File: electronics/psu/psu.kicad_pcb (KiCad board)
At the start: 2 copper layers, 100 x 100 mm, 65 parts, among them J1 Conn_01x03_Female, J2 control board, J3 processing, J4 processing, J5 pedals, J6 FAN, Q1 PHB21N06LT, U1 MC7815, U2 MC7915, U3 MIC4684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

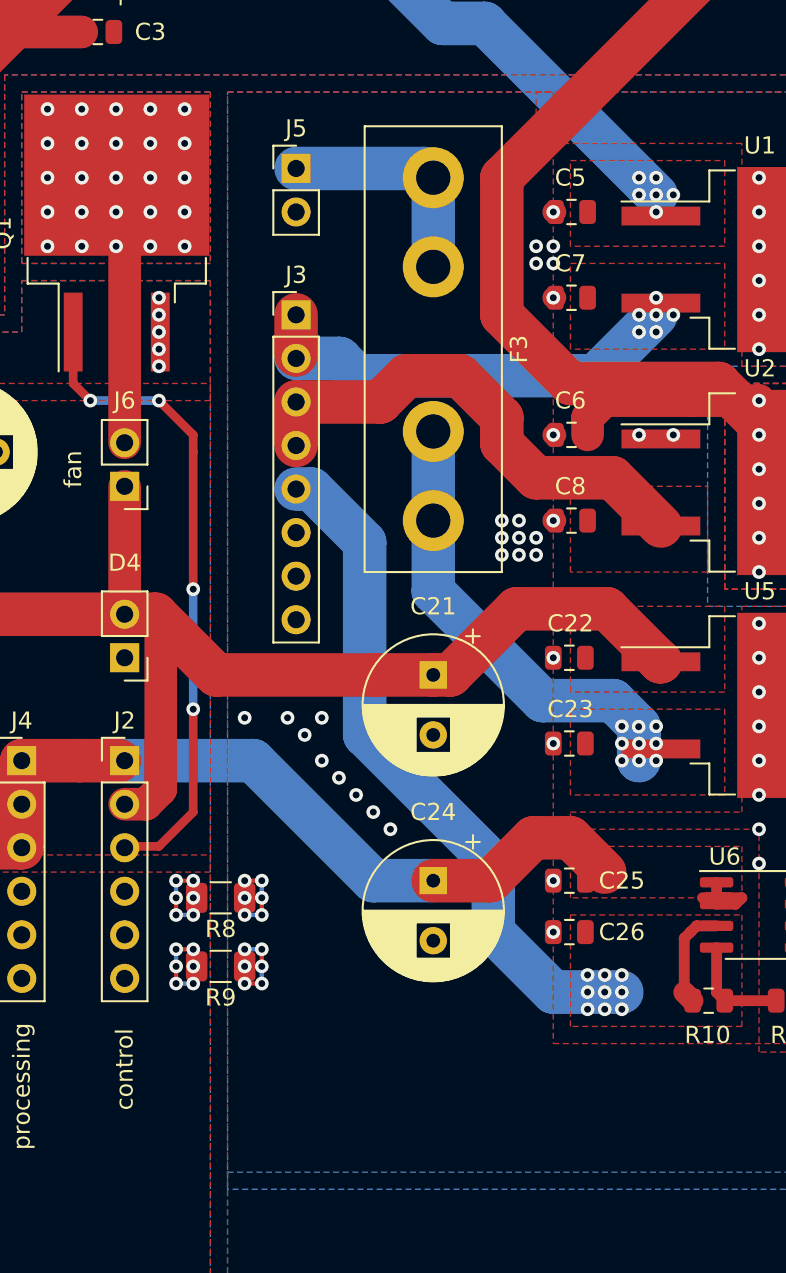
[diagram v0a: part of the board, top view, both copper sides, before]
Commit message: Changement de la fuse pour le 9v par une efuse
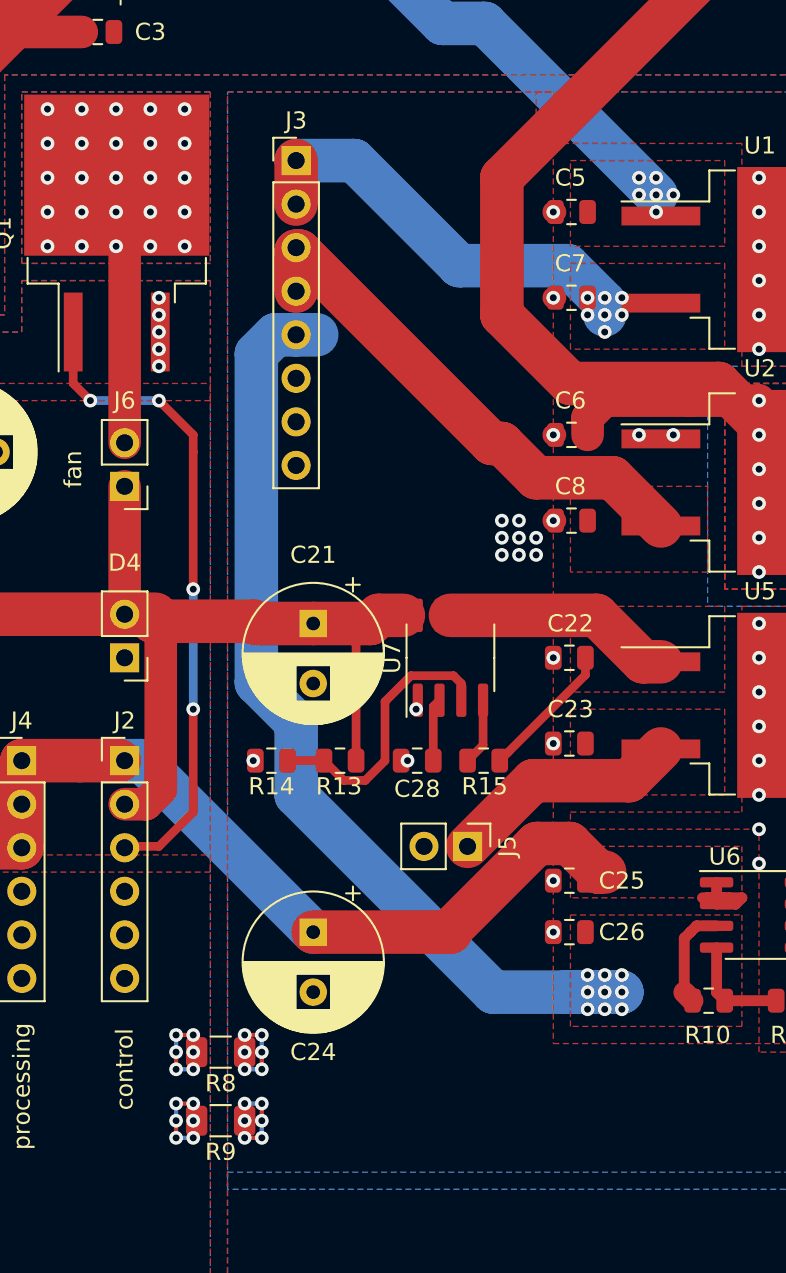
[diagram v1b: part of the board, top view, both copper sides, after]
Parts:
- removed F3: 0.5A, bass_amplifier:M205_FUSE
- added C28: C, Capacitor_SMD:C_0805_2012Metric, F.Cu at (90.1, 89.0)
- added R13: inf, Resistor_SMD:R_0805_2012Metric, F.Cu at (85.6, 89.0)
- added R14: inf, Resistor_SMD:R_0805_2012Metric, F.Cu at (81.6, 89.0)
- added R15: 309, Resistor_SMD:R_0805_2012Metric, F.Cu at (93.9, 89.0)
- added U7: NIS5112, Package_SO:SOIC-8_3.9x4.9mm_P1.27mm, F.Cu at (92.0, 83.0)
- moved J5 40.8 mm to (93.0, 94.0), turned to 270 degrees
- moved J3 9.00 mm to (83.0, 54.0)
- moved R8 9.00 mm to (78.6, 106.0)
- moved R9 9.00 mm to (78.6, 110.0)
- moved C21 7.62 mm to (84.0, 81.0)
- moved C24 7.62 mm to (84.0, 99.0)
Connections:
- C22 pad 1: /D+12V -> Net-(C22-Pad1)
- C23 pad 1: Net-(C23-Pad1) -> /A+9V
- U5 pad 1: /D+12V -> Net-(C22-Pad1)
- U5 pad 3: Net-(C23-Pad1) -> /A+9V
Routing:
- net Net-(C23-Pad1): track 27.6 -> 0.00 mm, vias 9 -> 0
- net Net-(C22-Pad1): track 0.00 -> 21.5 mm
- net /A+3.3V: track 46.1 -> 66.0 mm
- net Net-(R13-Pad1): track 0.00 -> 16.3 mm
- net /D+12V: track 90.9 -> 82.4 mm
- net Net-(R15-Pad1): track 0.00 -> 3.90 mm
- net Net-(C28-Pad1): track 0.00 -> 3.68 mm
- net /A+15V: track 27.8 -> 24.7 mm, vias 6 -> 7
- net /D+5V: track 81.3 -> 83.5 mm
- net /A-15V: track 29.0 -> 30.3 mm
- net GNDA: vias 194 -> 184
- added copper zone on F.Cu, net /A+9V
- added copper zone on F.Cu, net Net-(C22-Pad1)
- removed copper zone on F.Cu, net Net-(C23-Pad1)

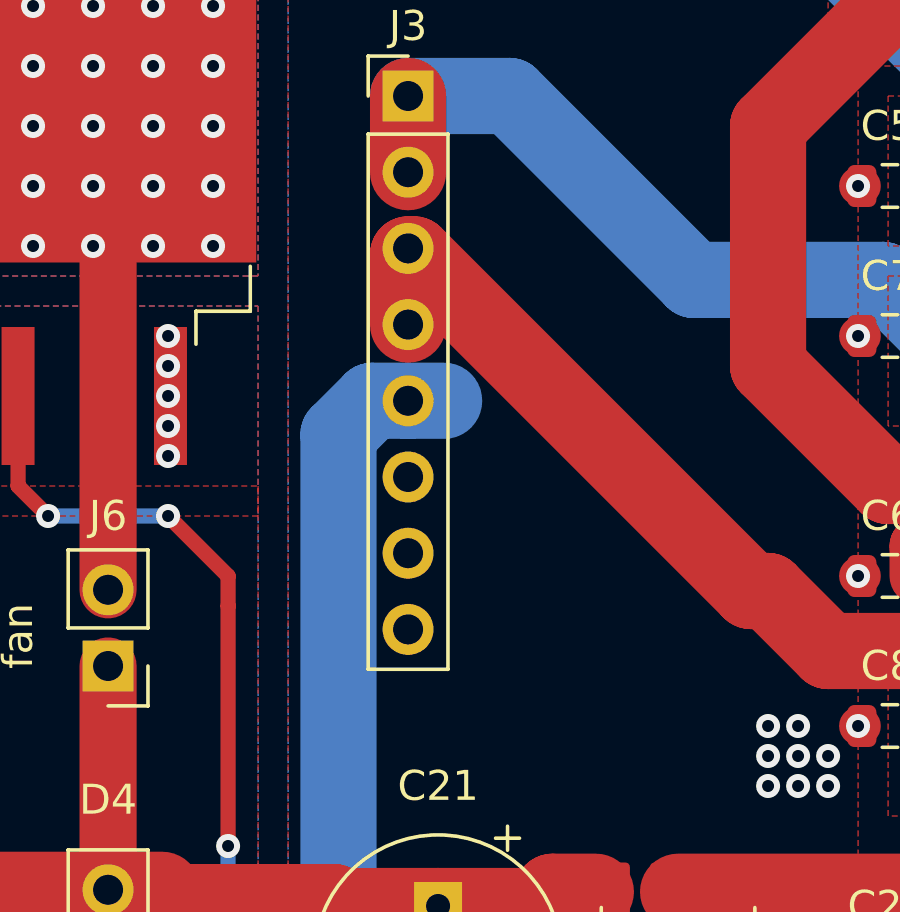
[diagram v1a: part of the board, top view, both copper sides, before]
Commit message: Correction d'erreurs dans PSU
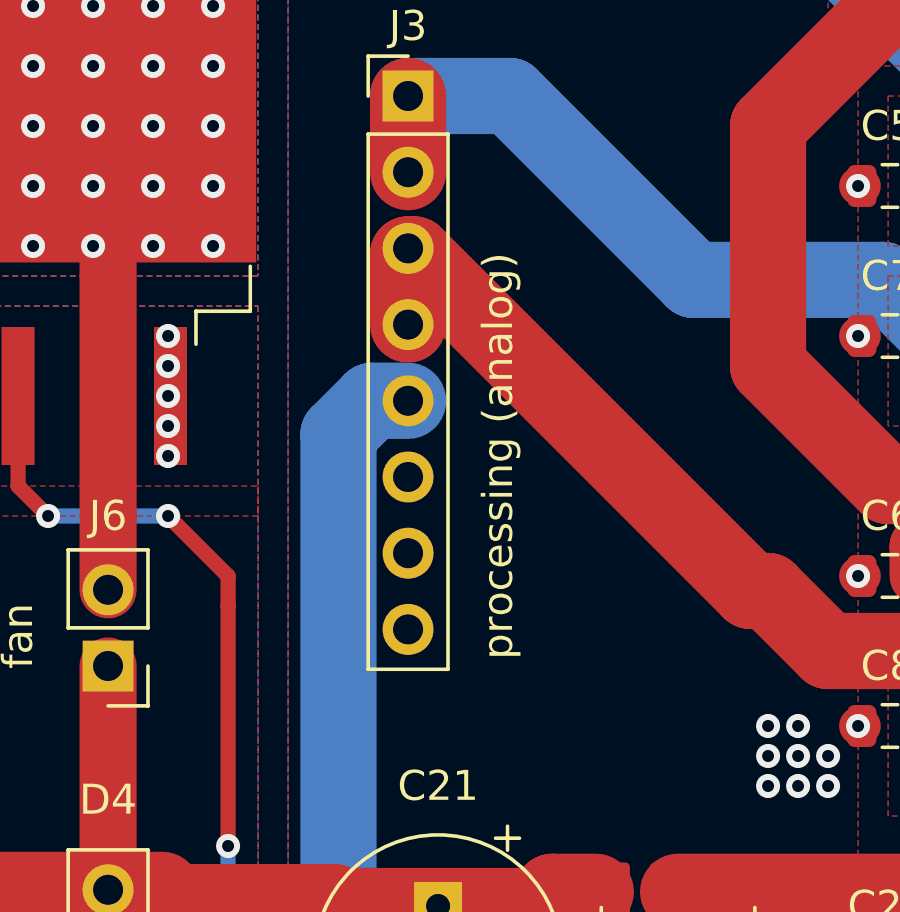
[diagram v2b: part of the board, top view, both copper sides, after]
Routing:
- net /A+3.3V: track 66.0 -> 64.8 mm
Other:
- board text added: "processing (analog)"
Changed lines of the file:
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@@
   (general
     (thickness 1.6)
-    (drawings 7)
-    (tracks 710)
+    (drawings 8)
+    (tracks 709)
     (zones 0)
     (modules 69)
@@
   )
   (setup
-    (last_trace_width 2.54)
+    (last_trace_width 0.25)
     (user_trace_width 0.381)
     (user_trace_width 0.508)
@@
     (pad 1 np_thru_hole circle (at 0 0) (size 3.2 3.2) (drill 3.2) (layers *.Cu *.Mask))
   )
+  (gr_text "processing (analog)" (at 86 66 90) (layer F.SilkS)
+    (effects (font (size 1 1) (thickness 0.15)))
+  )
   (gr_text control (at 73 107 90) (layer F.SilkS)
     (effects (font (size 1 1) (thickness 0.15)))
@@
   (via (at 102 103.5) (size 0.8) (drill 0.4) (layers F.Cu B.Cu) (net 15))
   (via (at 102 102.5) (size 0.8) (drill 0.4) (layers F.Cu B.Cu) (net 15))
-  (segment (start 84.202081 64.16) (end 83 64.16) (width 2.54) (layer B.Cu) (net 15))
   (segment (start 100.434315 102.5) (end 101 102.5) (width 2.54) (layer B.Cu) (net 15))
   (segment (start 98.732398 102.5) (end 100.434315 102.5) (width 2.54) (layer B.Cu) (net 15))

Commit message: Ajout des fichiers gerber pour le projet psu.
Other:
- board text added: "G/+9"
- board text added: "G/G/G/+3.3/-15/-15/+15/+15"
- board text added: "G/G/G/+5/+5/+5"
- board text added: "G/G/G/fan/+12/+5"
- board text added: "LED(-/+)"
- board text added: "fan(+/-)"
- board text added: "~~/G/~~"
- board text removed: "fan"
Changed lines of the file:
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@@
   (general
     (thickness 1.6)
-    (drawings 8)
+    (drawings 14)
     (tracks 709)
     (zones 0)
@@
     (visible_elements FFFDFF7F)
     (pcbplotparams
-      (layerselection 0x010fc_ffffffff)
-      (usegerberextensions false)
+      (layerselection 0x010f0_ffffffff)
+      (usegerberextensions true)
       (usegerberattributes false)
       (usegerberadvancedattributes false)
@@
       (outputformat 1)
       (mirror false)
-      (drillshape 1)
+      (drillshape 0)
       (scaleselection 1)
-      (outputdirectory ""))
+      (outputdirectory "gerber/"))
   )
   (net 0 "")
@@
   (module bass_amplifier:transformer_connector (layer F.Cu)
     (at 31 42 90)
-    (fp_text reference J1 (at 0 -3 90) (layer F.SilkS)
+    (fp_text reference J1 (at 12 -3 90) (layer F.SilkS)
       (effects (font (size 1 1) (thickness 0.15)))
     )
@@
     (pad 1 np_thru_hole circle (at 0 0) (size 3.2 3.2) (drill 3.2) (layers *.Cu *.Mask))
   )
+  (gr_text G/+9 (at 92 97) (layer F.SilkS)
+    (effects (font (size 1 1) (thickness 0.15)))
+  )
+  (gr_text G/G/G/+3.3/-15/-15/+15/+15 (at 88 63 90) (layer F.SilkS)
+    (effects (font (size 1 1) (thickness 0.15)))
+  )
+  (gr_text ~~/G/~~ (at 30 30 90) (layer F.SilkS)
+    (effects (font (size 1 1) (thickness 0.15)))
+  )
+  (gr_text G/G/G/+5/+5/+5 (at 68 111 90) (layer F.SilkS)
+    (effects (font (size 1 1) (thickness 0.15)))
+  )
+  (gr_text G/G/G/fan/+12/+5 (at 74 112 90) (layer F.SilkS)
+    (effects (font (size 1 1) (thickness 0.15)))
+  )
+  (gr_text "LED(-/+)" (at 70 82 90) (layer F.SilkS)
+    (effects (font (size 1 1) (thickness 0.15)))
+  )
   (gr_text "processing (analog)" (at 86 66 90) (layer F.SilkS)
     (effects (font (size 1 1) (thickness 0.15)))
   )
-  (gr_text control (at 73 107 90) (layer F.SilkS)
+  (gr_text control (at 72 107 90) (layer F.SilkS)
     (effects (font (size 1 1) (thickness 0.15)))
   )
-  (gr_text fan (at 70 72 90) (layer F.SilkS)
+  (gr_text "fan(+/-)" (at 70 72 90) (layer F.SilkS)
     (effects (font (size 1 1) (thickness 0.15)))
   )
-  (gr_text processing (at 67 108 90) (layer F.SilkS)
+  (gr_text processing (at 66 108 90) (layer F.SilkS)
     (effects (font (size 1 1) (thickness 0.15)))
   )
